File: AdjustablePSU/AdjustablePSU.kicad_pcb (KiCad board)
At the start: 2 copper layers, 88.9 x 68.6 mm, 30 parts

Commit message: Docs created
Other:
- board text added: "AC INPUT"
- board text added: "DC OUTPUT"
- board text removed: "AC INPUT ONLY!"
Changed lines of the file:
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@@
   (general
     (thickness 1.6)
-    (drawings 20)
+    (drawings 39)
     (tracks 135)
     (zones 0)
@@
     (descr "LED, diameter 5.0mm, 2 pins, http://cdn-reichelt.de/documents/datenblatt/A500/LL-504BC2E-009.pdf")
     (tags "LED diameter 5.0mm 2 pins")
-    (fp_text reference D_NEG4 (at 1.016 3.81 180) (layer F.SilkS)
+    (fp_text reference D_NEG4 (at 1.016 3.81) (layer F.SilkS)
       (effects (font (size 0.4 0.4) (thickness 0.1)))
     )
@@
     )
   )
+  (gr_line (start 141.732 79.248) (end 141.732 73.152) (layer F.SilkS) (width 0.3))
+  (gr_line (start 155.448 79.248) (end 141.732 79.248) (layer F.SilkS) (width 0.3))
+  (gr_line (start 155.448 73.152) (end 155.448 79.248) (layer F.SilkS) (width 0.3))
+  (gr_line (start 141.732 73.152) (end 155.448 73.152) (layer F.SilkS) (width 0.3))
+  (gr_line (start 112.268 76.962) (end 106.172 76.962) (layer F.SilkS) (width 0.3))
+  (gr_line (start 112.268 80.518) (end 112.268 76.962) (layer F.SilkS) (width 0.3))
+  (gr_line (start 106.172 80.518) (end 112.268 80.518) (layer F.SilkS) (width 0.3))
+  (gr_line (start 106.172 76.962) (end 106.172 80.518) (layer F.SilkS) (width 0.3))
+  (gr_line (start 107.315 75.565) (end 106.68 75.946) (layer F.SilkS) (width 0.2))
+  (gr_line (start 107.315 74.93) (end 107.315 75.565) (layer F.SilkS) (width 0.2))
+  (gr_line (start 104.775 74.295) (end 107.315 75.565) (layer F.SilkS) (width 0.2))
+  (gr_line (start 104.775 65.151) (end 104.775 74.295) (layer F.SilkS) (width 0.2))
+  (gr_line (start 164.465 78.105) (end 163.83 78.74) (layer F.SilkS) (width 0.2))
+  (gr_line (start 164.465 78.105) (end 163.83 77.47) (layer F.SilkS) (width 0.2))
+  (gr_line (start 164.465 74.295) (end 163.83 74.93) (layer F.SilkS) (width 0.2))
+  (gr_line (start 164.465 74.295) (end 163.83 73.66) (layer F.SilkS) (width 0.2))
+  (gr_line (start 156.845 78.105) (end 164.465 78.105) (layer F.SilkS) (width 0.2))
+  (gr_line (start 156.845 74.295) (end 164.465 74.295) (layer F.SilkS) (width 0.2))
+  (gr_text "DC OUTPUT" (at 160.655 76.2) (layer F.SilkS)
+    (effects (font (size 1 1) (thickness 0.1)))
+  )
   (gr_line (start 168.79082 60.796608) (end 169.55282 61.558608) (layer F.SilkS) (width 0.3))
   (gr_line (start 168.79082 60.796608) (end 168.02882 61.558608) (layer F.SilkS) (width 0.3))
@@
   (gr_line (start 130.18282 55.970608) (end 130.18282 64.098608) (layer F.SilkS) (width 0.2))
   (gr_line (start 167.01282 55.970608) (end 167.01282 64.098608) (layer F.SilkS) (width 0.2))
-  (gr_text "AC INPUT\nONLY!" (at 105.918 72.39 270) (layer F.SilkS)
+  (gr_text "AC \nINPUT" (at 106.426 63.246) (layer F.SilkS)
     (effects (font (size 1 1) (thickness 0.1) italic))
   )

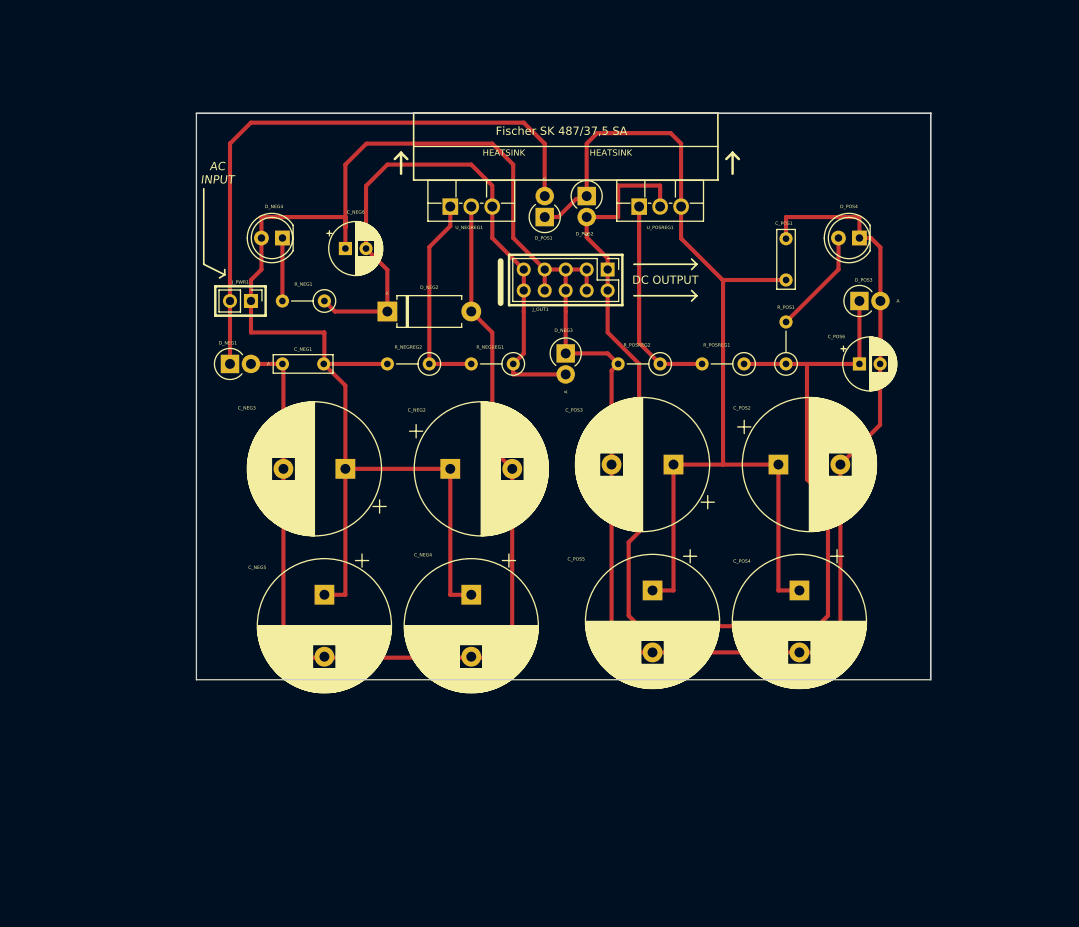
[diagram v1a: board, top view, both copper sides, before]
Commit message: Changed Adjustable design to use ground plane
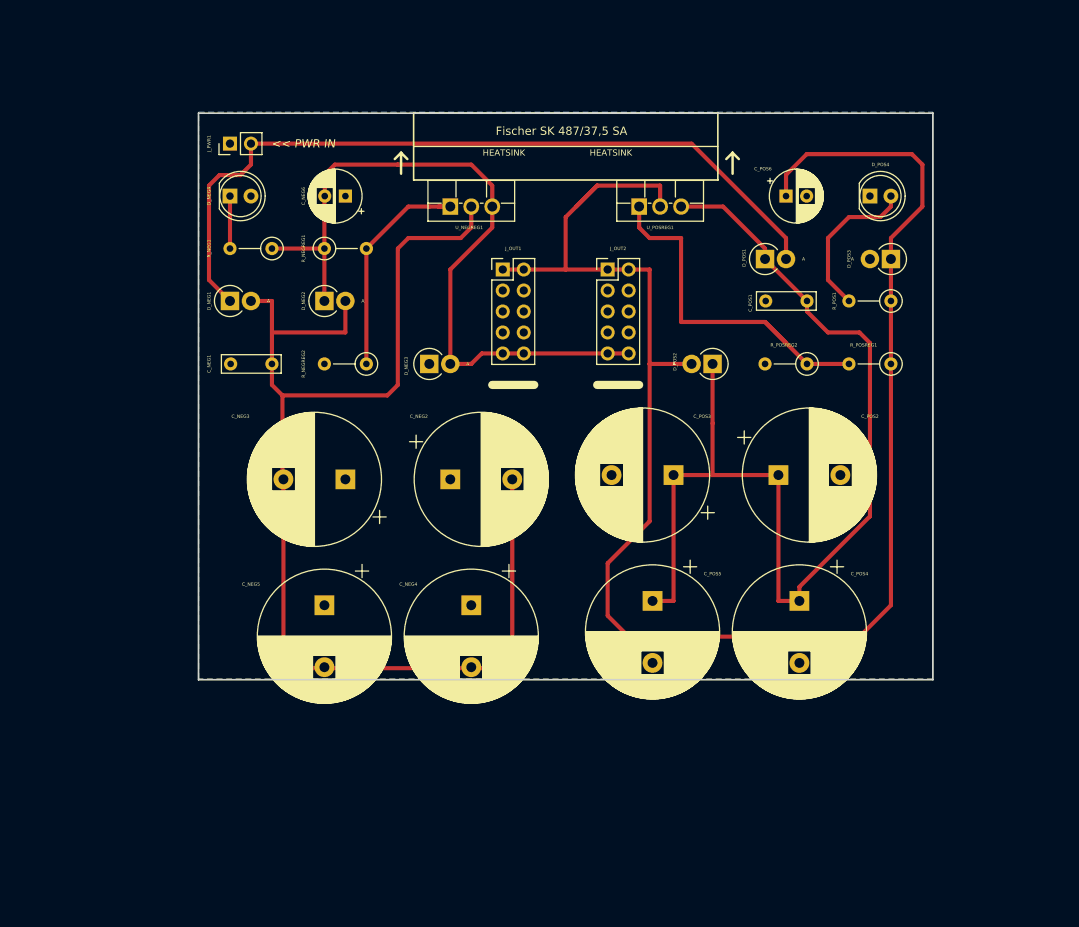
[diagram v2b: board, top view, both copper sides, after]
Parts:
- added J_OUT2: Conn_02x05_Odd_Even, Connector_PinHeader_2.54mm:PinHeader_2x05_P2.54mm_Vertical, F.Cu at (153.7, 74.9)
- D_NEG2: footprint Diode_THT:D_DO-15_P10.16mm_Horizontal -> Diode_THT:D_DO-15_P2.54mm_Vertical_AnodeUp
- moved D_POS1 27.1 mm to (172.7, 73.7), turned to 0 degrees
- moved R_NEGREG1 26.8 mm to (119.4, 72.4), turned to 0 degrees
- moved D_POS2 25.4 mm to (166.4, 86.4), turned to 180 degrees
- moved C_POS6 22.2 mm to (175.3, 66.0)
- moved J_PWR1 19.2 mm to (108.0, 59.7), turned to 90 degrees
- moved R_POSREG1 17.8 mm to (188.0, 86.4)
- moved R_POSREG2 17.8 mm to (177.8, 86.4)
- moved D_NEG3 16.6 mm to (132.1, 86.4), turned to 0 degrees
- moved R_POS1 14.8 mm to (188.0, 78.7), turned to 180 degrees
- moved J_OUT1 12.7 mm to (141.0, 74.9), turned to 0 degrees
- moved R_NEG1 8.98 mm to (113.0, 72.4)
- moved D_NEG4 8.13 mm to (108.0, 66.0), turned to 0 degrees
- moved D_NEG2 7.73 mm to (119.4, 78.7)
- moved R_NEGREG2 7.62 mm to (124.5, 86.4)
- moved D_NEG1 7.62 mm to (108.0, 78.7)
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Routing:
- net GND: track 313.5 -> 0.05 mm
- net /12VDC_POS_REG: track 145.0 -> 204.8 mm
- net /DC_NEG_IN: track 123.9 -> 154.4 mm
- net /AC_IN: track 73.2 -> 95.7 mm
- net Net-(R_POSREG1-Pad2): track 25.2 -> 44.3 mm
- net /12VDC_NEG_REG: track 73.1 -> 89.3 mm
- net Net-(D_POS4-Pad2): track 12.8 -> 19.1 mm
- net /DC_POS_IN: track 121.8 -> 127.7 mm
- net Net-(R_NEGREG1-Pad2): track 25.2 -> 27.7 mm
- net Net-(D_NEG4-Pad1): track 7.62 -> 6.35 mm
- added copper zone on B.Cu, net GND
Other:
- board text added: "<< PWR IN"
- board text removed: "AC INPUT"
- board text removed: "DC OUTPUT"

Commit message: Updated silkscreen
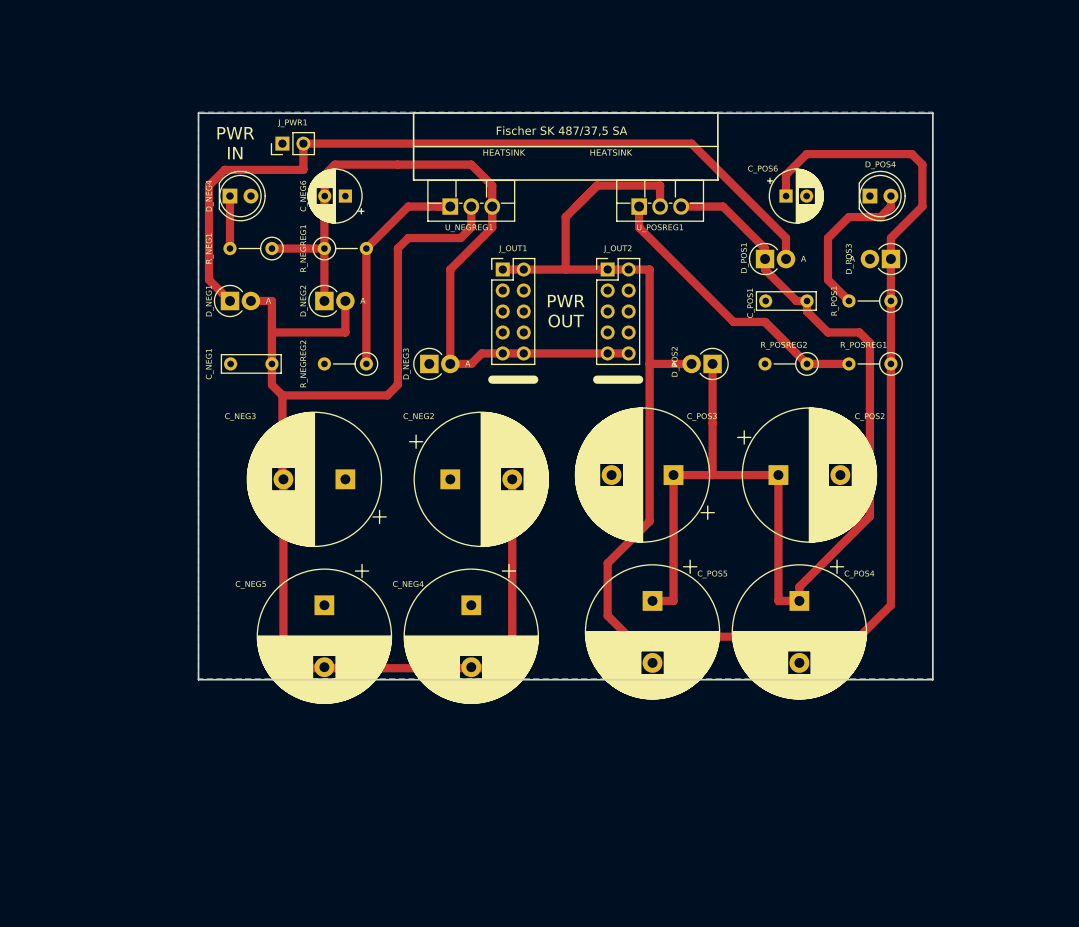
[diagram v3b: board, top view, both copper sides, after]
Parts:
- moved J_PWR1 6.35 mm to (114.3, 59.7)
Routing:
- net Net-(R_POSREG1-Pad2): track 44.3 -> 38.4 mm
- net /DC_POS_IN: track 127.7 -> 128.4 mm
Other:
- net class Default: trace_width 0.25 -> 1
- board text added: "PWR IN"
- board text added: "PWR OUT"
- board text added: "R1"
- board text added: "R2"
- board text added: "Regulated Output Voltage ————————————————— R1=120R R2=390R Vout=5.3V R1=120R R2=750R Vout=9.1V R1=120R R2=1K Vout=11.6V R1=150R R2=2K Vout=17.9V R1=120R R2=2K2 Vout=24.1V"
- board text removed: "<< PWR IN"

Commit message: Finished RevA board
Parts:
- added REF**: MountingHole_3.2mm_M3_ISO14580, MountingHole:MountingHole_3.2mm_M3_ISO14580, F.Cu at (107.3, 123.8)
- added REF**: MountingHole_3.2mm_M3_ISO14580, MountingHole:MountingHole_3.2mm_M3_ISO14580, F.Cu at (189.9, 123.8)
- added REF**: MountingHole_3.2mm_M3_ISO14580, MountingHole:MountingHole_3.2mm_M3_ISO14580, F.Cu at (189.9, 59.1)
- added REF**: MountingHole_3.2mm_M3_ISO14580, MountingHole:MountingHole_3.2mm_M3_ISO14580, F.Cu at (107.3, 59.1)
- added REF**: MountingHole_3.2mm_M3_ISO14580, MountingHole:MountingHole_3.2mm_M3_ISO14580, F.Cu at (154.9, 59.7)
- added REF**: MountingHole_3.2mm_M3_ISO14580, MountingHole:MountingHole_3.2mm_M3_ISO14580, F.Cu at (142.9, 59.7)
- added REF**: MountingHole_3.2mm_M3_ISO14580, MountingHole:MountingHole_3.2mm_M3_ISO14580, F.Cu at (130.8, 59.7)
- added REF**: MountingHole_3.2mm_M3_ISO14580, MountingHole:MountingHole_3.2mm_M3_ISO14580, F.Cu at (167.6, 59.7)
- moved R_NEGREG1 16.8 mm to (108.3, 85.1)
- moved C_NEG1 15.0 mm to (125.1, 77.5), turned to 0 degrees
- moved D_NEG2 12.1 mm to (127.6, 69.8), turned to 180 degrees
- moved C_POS1 11.8 mm to (166.1, 77.5), turned to 0 degrees
- moved R_NEG1 7.65 mm to (118.7, 77.5)
- moved D_POS1 7.62 mm to (166.1, 69.8)
- moved R_POS1 7.22 mm to (180.8, 77.5)
- moved C_NEG6 6.87 mm to (116.2, 69.8), turned to 0 degrees
- moved U_NEGREG1 5.08 mm to (139.7, 67.3)
- moved C_POS5 5.06 mm to (162.6, 118.7), turned to 180 degrees
- moved C_NEG4 4.96 mm to (133.3, 118.7), turned to 0 degrees
- moved C_POS6 4.58 mm to (177.8, 69.8)
- moved D_POS4 4.58 mm to (188.0, 69.8), turned to 180 degrees
- moved U_POSREG1 4.44 mm to (153.0, 67.3)
- moved D_POS3 4.32 mm to (185.9, 77.5), turned to 0 degrees
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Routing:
- net /DC_NEG_IN: track 154.4 -> 192.6 mm
- net /12VDC_NEG_REG: track 89.3 -> 109.3 mm
- net Net-(R_NEGREG1-Pad2): track 27.7 -> 41.6 mm
- net /DC_POS_IN: track 128.4 -> 136.8 mm
- net /AC_IN: track 96.1 -> 101.4 mm
- net /12VDC_POS_REG: track 204.8 -> 200.7 mm
- net Net-(D_NEG4-Pad1): track 6.35 -> 9.99 mm
- net Net-(D_POS4-Pad2): track 19.1 -> 16.2 mm
- net Net-(R_POSREG1-Pad2): track 38.4 -> 40.9 mm
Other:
- board size 88.9 x 68.6 mm -> 88.9 x 71 mm
- board text added: "+/- 5V +/- 9V +/- 12V +/- 18V +/- 24V"
- board text added: "Heatsink Thermal Ω < 10 K/W"
- board text added: "Linear Bipolar PSU"
- board text added: "R1=120R R1=120R R1=120R R1=150R R1=120R"
- board text added: "R2=390R R2=750R R2=1K1 R2=2K R2=2K2"
- board text added: "RevA 2018 Chris Sutton"
- board text added: "‘Programmable’ Regulator Output"
- board text removed: "Fischer SK 487/37,5 SA"
- board text removed: "Regulated Output Voltage ————————————————— R1=120R R2=390R Vout=5.3V R1=120R R2=750R Vout=9.1V R1=120R R2=1K Vout=11.6V R1=150R R2=2K Vout=17.9V R1=120R R2=2K2 Vout=24.1V"

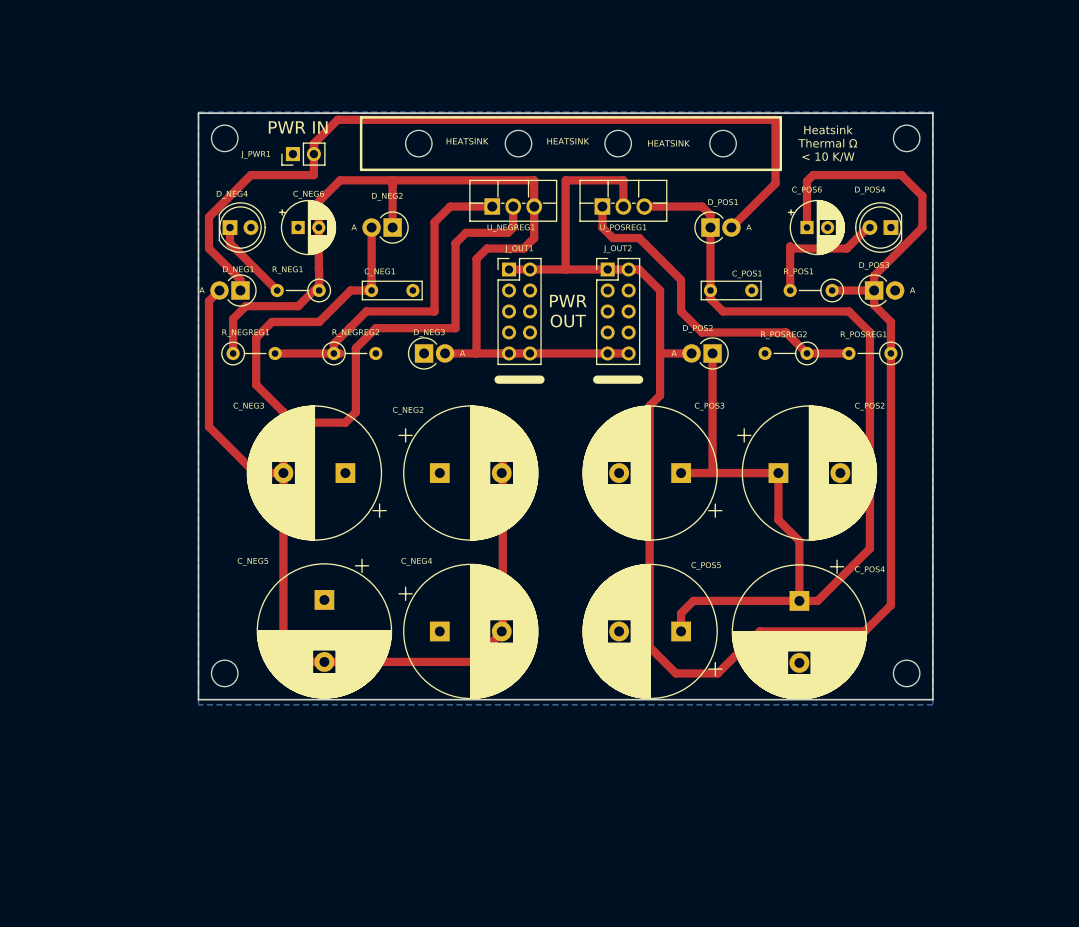
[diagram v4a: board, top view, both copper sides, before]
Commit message: Created SMT version of AdjustablePSU, RevB
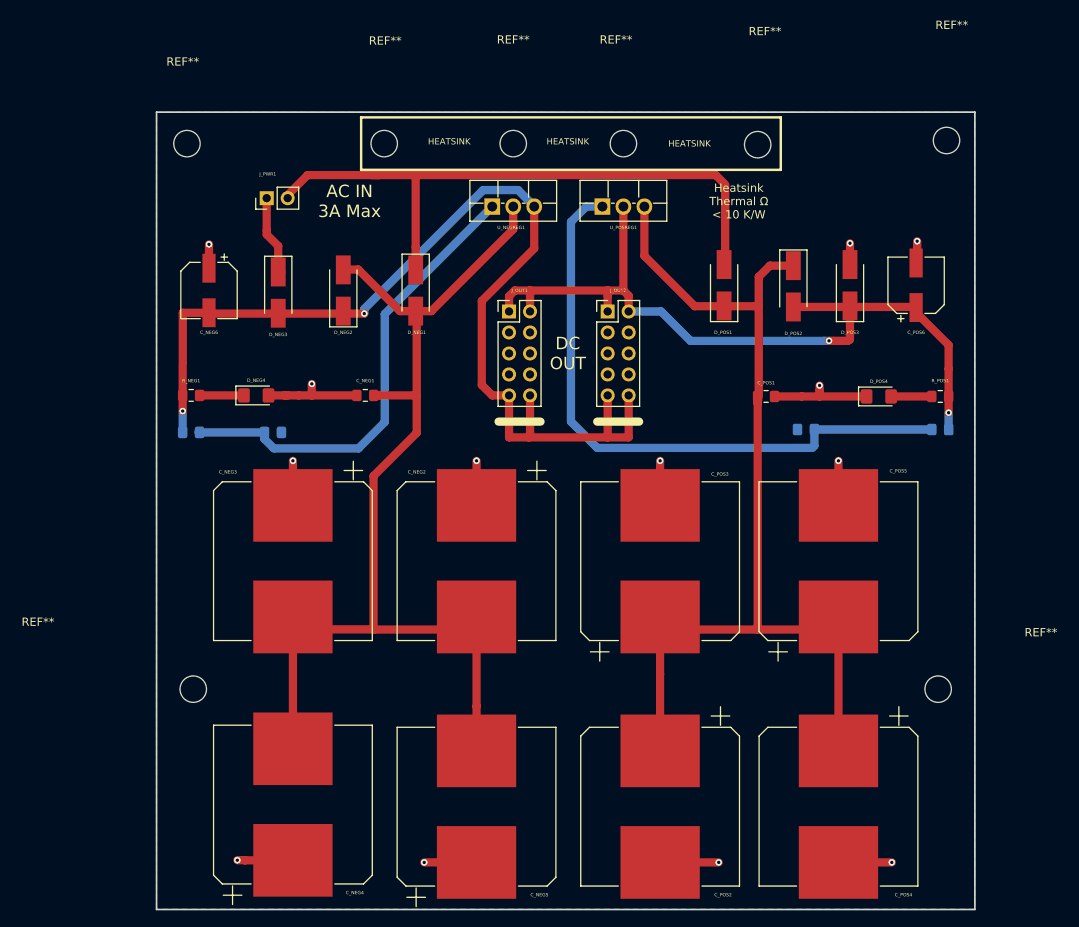
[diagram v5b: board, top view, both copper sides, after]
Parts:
- removed the REF** at (107.3, 123.8)
- removed the REF** at (189.9, 123.8)
- removed the REF** at (189.9, 59.1)
- removed the REF** at (107.3, 59.1)
- removed the REF** at (154.9, 59.7)
- removed the REF** at (142.9, 59.7)
- removed the REF** at (130.8, 59.7)
- removed the REF** at (167.6, 59.7)
- added REF**: MountingHole_3.2mm_M3, MountingHole:MountingHole_3.2mm_M3, F.Cu at (171.8, 59.8)
- added REF**: MountingHole_3.2mm_M3, MountingHole:MountingHole_3.2mm_M3, F.Cu at (126.6, 59.7)
- added REF**: MountingHole_3.2mm_M3, MountingHole:MountingHole_3.2mm_M3, F.Cu at (102.7, 59.7)
- added REF**: MountingHole_3.2mm_M3, MountingHole:MountingHole_3.2mm_M3, F.Cu at (194.7, 59.3)
- added REF**: MountingHole_3.2mm_M3, MountingHole:MountingHole_3.2mm_M3, F.Cu at (193.7, 125.7)
- added REF**: MountingHole_3.2mm_M3, MountingHole:MountingHole_3.2mm_M3, F.Cu at (103.5, 125.7)
- added REF**: MountingHole_3.2mm_M3, MountingHole:MountingHole_3.2mm_M3, F.Cu at (142.2, 59.7)
- added REF**: MountingHole_3.2mm_M3, MountingHole:MountingHole_3.2mm_M3, F.Cu at (155.6, 59.7)
- C_NEG1, C_POS1: footprint Capacitor_THT:C_Rect_L7.0mm_W2.0mm_P5.00mm -> Capacitor_SMD:C_0805_2012Metric_Pad1.15x1.40mm_HandSolder
- C_NEG2, C_NEG3, C_NEG4, C_NEG5, C_POS2, C_POS3, C_POS4, C_POS5: value 4700uF -> 3300uF; footprint Capacitor_THT:CP_Radial_D16.0mm_P7.50mm -> Capacitor_SMD:CP_Elec_18x22
- C_NEG6, C_POS6: footprint Capacitor_THT:CP_Radial_D6.3mm_P2.50mm -> Capacitor_SMD:CP_Elec_6.3x3.9
- D_NEG1: value 1N4007 -> HER202G; footprint Diode_THT:D_DO-15_P2.54mm_Vertical_AnodeUp -> Diode_SMD:D_SMA_Handsoldering
- D_NEG2, D_NEG3, D_POS1, D_POS2, D_POS3: value 1N4004 -> HER202G; footprint Diode_THT:D_DO-15_P2.54mm_Vertical_AnodeUp -> Diode_SMD:D_SMA_Handsoldering
- D_NEG4, D_POS4: footprint LED_THT:LED_D5.0mm -> LED_SMD:LED_1206_3216Metric_Pad1.42x1.75mm_HandSolder
- R_NEG1, R_POS1: footprint Resistor_THT:R_Axial_DIN0207_L6.3mm_D2.5mm_P5.08mm_Vertical -> Resistor_SMD:R_0805_2012Metric_Pad1.15x1.40mm_HandSolder
- R_NEGREG1, R_POSREG1: footprint Resistor_THT:R_Axial_DIN0207_L6.3mm_D2.5mm_P5.08mm_Vertical -> Resistor_SMD:R_0805_2012Metric_Pad1.15x1.40mm_HandSolder; moved to B.Cu
- R_NEGREG2, R_POSREG2: value 390R -> 1K1; footprint Resistor_THT:R_Axial_DIN0207_L6.3mm_D2.5mm_P5.08mm_Vertical -> Resistor_SMD:R_0805_2012Metric_Pad1.15x1.40mm_HandSolder; moved to B.Cu
- moved C_POS2 42.9 mm to (160.0, 140.0), turned to 270 degrees
- moved C_NEG5 31.1 mm to (137.8, 140.0), turned to 90 degrees
- moved C_NEG4 27.5 mm to (115.6, 139.7), turned to 90 degrees
- moved C_POS4 25.3 mm to (181.6, 140.0)
- moved D_NEG1 21.2 mm to (130.4, 77.5), turned to 270 degrees
- moved C_POS5 20.9 mm to (181.6, 110.2), turned to 90 degrees
- moved D_NEG4 20.6 mm to (111.1, 90.2)
- moved D_POS4 20.5 mm to (186.5, 90.3), turned to 0 degrees
- moved R_NEG1 20.0 mm to (103.3, 90.2), turned to 0 degrees
- moved D_NEG3 19.1 mm to (113.8, 77.7), turned to 270 degrees
- moved R_POS1 18.3 mm to (193.9, 90.3)
- moved C_POS6 14.9 mm to (191.0, 76.8), turned to 90 degrees
- moved C_POS1 14.5 mm to (172.8, 90.3)
- moved C_NEG6 13.2 mm to (105.4, 77.5), turned to 270 degrees
- moved C_NEG1 12.7 mm to (124.3, 90.2), turned to 180 degrees
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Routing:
- net /12VDC_POS_REG: track 200.7 -> 97.5 mm, vias 0 -> 2
- net GND: track 0.00 -> 90.1 mm, vias 0 -> 13
- net /DC_NEG_IN: track 192.6 -> 126.8 mm
- net Net-(R_POSREG1-Pad2): track 40.9 -> 75.8 mm
- net /AC_IN: track 101.4 -> 76.6 mm
- net /12VDC_NEG_REG: track 109.3 -> 127.0 mm, vias 0 -> 2
- net /DC_POS_IN: track 136.8 -> 121.1 mm
- net Net-(R_NEGREG1-Pad2): track 41.6 -> 56.6 mm
- net Net-(D_POS4-Pad2): track 16.2 -> 4.57 mm
- net Net-(D_NEG4-Pad1): track 9.99 -> 5.11 mm
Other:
- board size 88.9 x 71 mm -> 99.1 x 96.5 mm
- board text added: "+/- 5V +/- 9V +/- 12V +/- 15V"
- board text added: "AC IN 3A Max"
- board text added: "DC OUT"
- board text added: "Dual Power Supply"
- board text added: "R1=120R R1=120R R1=120R R1=180R"
- board text added: "R2=390R R2=750R R2=1K1 R2=2K"
- board text added: "RevB 0219 Chris Sutton"
- board text added: "‘Adjustable’ Regulator Output"
- board text removed: "+/- 5V +/- 9V +/- 12V +/- 18V +/- 24V"
- board text removed: "Linear Bipolar PSU"
- board text removed: "PWR IN"
- board text removed: "PWR OUT"
- board text removed: "R1=120R R1=120R R1=120R R1=150R R1=120R"
- board text removed: "R2=390R R2=750R R2=1K1 R2=2K R2=2K2"
- board text removed: "RevA 2018 Chris Sutton"
- board text removed: "‘Programmable’ Regulator Output"
